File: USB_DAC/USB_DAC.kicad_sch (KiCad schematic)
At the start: 65 parts, among them J1 USB_B, J2 DAC_OUT_L, J3 DAC_OUT_R, Q1 BC847C, U1 MIC5205YM5, U2 USBLC6-2SC6, U3 OPA2353UA, U4 PCM2900, Y1 12MHz 18pF

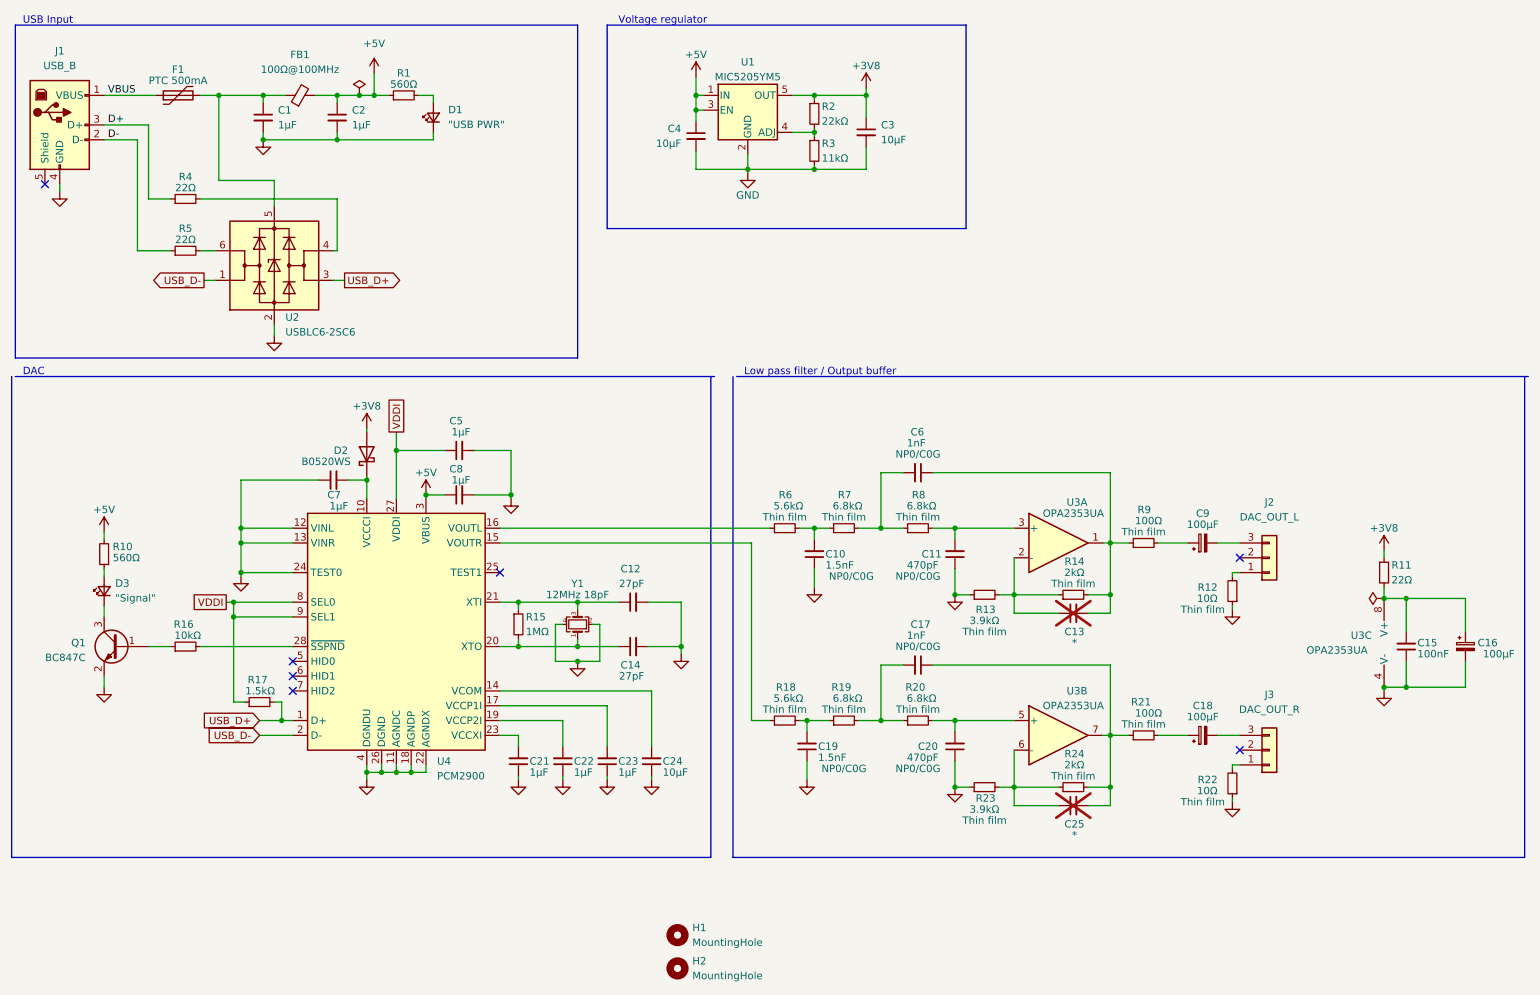
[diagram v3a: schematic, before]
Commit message: Updated component values
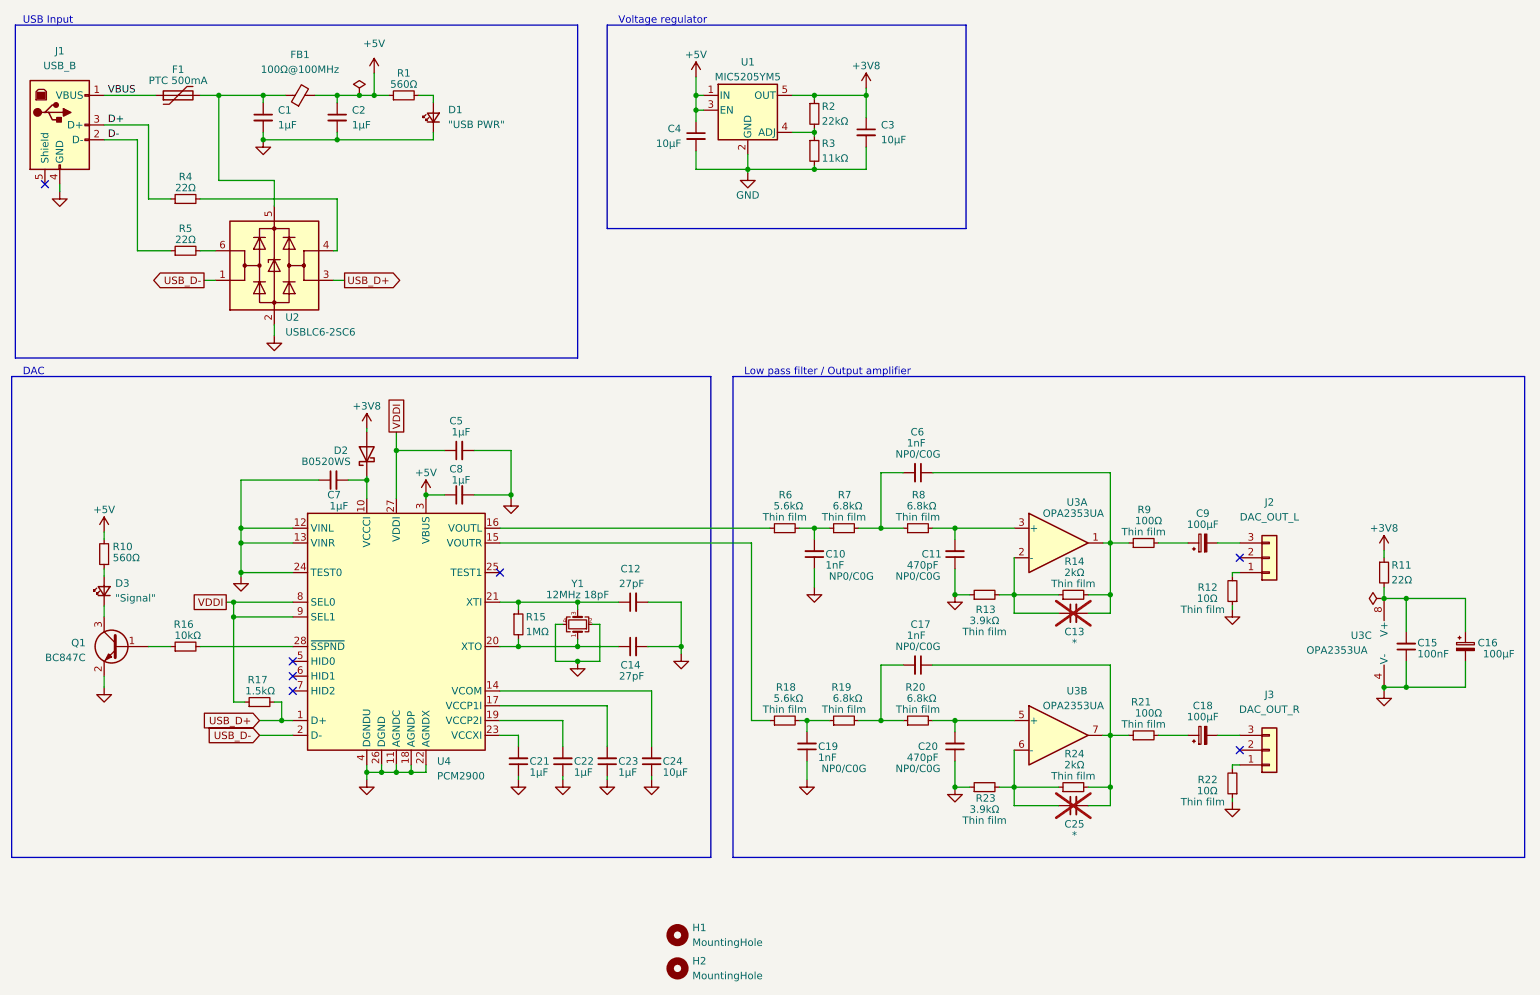
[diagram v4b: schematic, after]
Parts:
- C10, C19: value 1.5nF -> 1nF
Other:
- note added: "Low pass filter / Output amplifier"
- note removed: "Low pass filter / Output buffer"
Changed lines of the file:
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@@
     (stroke (width 0) (type default))
   )
-  (polyline (pts (xy 17.145 79.375) (xy 137.16 79.375))
+  (polyline (pts (xy 16.51 79.375) (xy 136.525 79.375))
     (stroke (width 0) (type default))
   )
@@
     (stroke (width 0) (type default))
   )
-  (polyline (pts (xy 140.97 79.375) (xy 276.86 79.375))
+  (polyline (pts (xy 140.335 79.375) (xy 276.225 79.375))
     (stroke (width 0) (type default))
   )
@@
     (effects (font (size 1.27 1.27)) (justify left bottom))
   )
-  (text "Low pass filter / Output buffer" (at 142.24 79.375 0)
+  (text "Low pass filter / Output amplifier" (at 142.24 79.375 0)
     (effects (font (size 1.27 1.27)) (justify left bottom))
   )
@@
       (effects (font (size 1.27 1.27)) (justify left))
     )
-    (property "Value" "1.5nF" (at 154.94 144.78 0)
+    (property "Value" "1nF" (at 154.94 144.78 0)
       (effects (font (size 1.27 1.27)) (justify left))
     )
@@
       (effects (font (size 1.27 1.27)) (justify left))
     )
-    (property "Value" "1.5nF" (at 156.21 111.76 0)
-      (effects (font (size 1.27 1.27)) (justify left))
-    )
+    (property "Value" "1nF" (at 156.21 111.76 0)
+      (effects (font (size 1.27 1.27)) (justify left))
+    )
